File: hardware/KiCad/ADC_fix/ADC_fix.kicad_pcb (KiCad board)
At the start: 2 copper layers, 8.2 x 13.7 mm, 3 parts, among them U1 MCP3422Axx-xMS, U2 MCP3423x-xUN

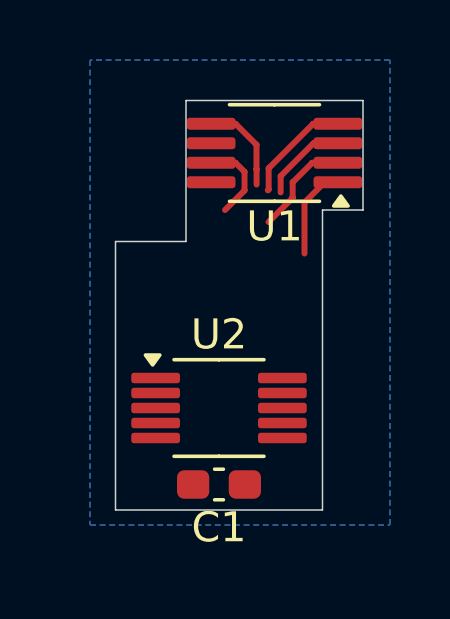
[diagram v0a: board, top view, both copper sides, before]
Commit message: Added ADC fix flex PCB design
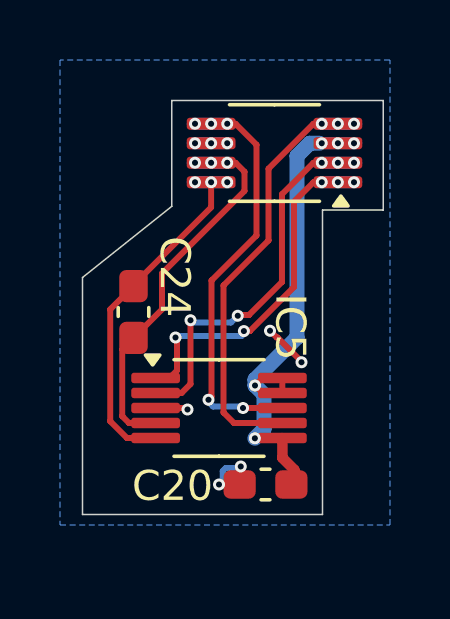
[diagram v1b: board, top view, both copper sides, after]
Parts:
- added C24: 100n, Capacitor_SMD:C_0603_1608Metric_Pad1.08x0.95mm_HandSolder, F.Cu at (151.4, 113.4)
- C20: renamed from C1; value C_Small -> 10n
- moved C20 1.55 mm to (155.8, 119.2)
- renumbered U2 to IC5, U1 to U5
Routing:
- net VDD: track 2.91 -> 16.4 mm, vias 0 -> 5
- net /CH2-: track 0.00 -> 11.1 mm, vias 0 -> 3
- net /SCL: track 3.13 -> 13.6 mm, vias 0 -> 5
- net /SDA: track 3.67 -> 13.8 mm, vias 0 -> 3
- net /CH2+: track 2.78 -> 12.3 mm, vias 0 -> 3
- net /CH1-: track 3.43 -> 12.3 mm, vias 0 -> 5
- net /CH1+: track 3.09 -> 11.2 mm, vias 0 -> 5
- net VSS: track 0.00 -> 4.55 mm, vias 0 -> 8
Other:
- board size 8.2 x 13.7 mm -> 10 x 13.8 mm
